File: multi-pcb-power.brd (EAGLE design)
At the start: 51.7 x 36.8 mm, 22 parts, among them Q5 TIP136, T2 BC618, X1 2.52B-ZR, X2 2.52B-ZR, X3 2.52B-ZR, X4 2.54B-ZR

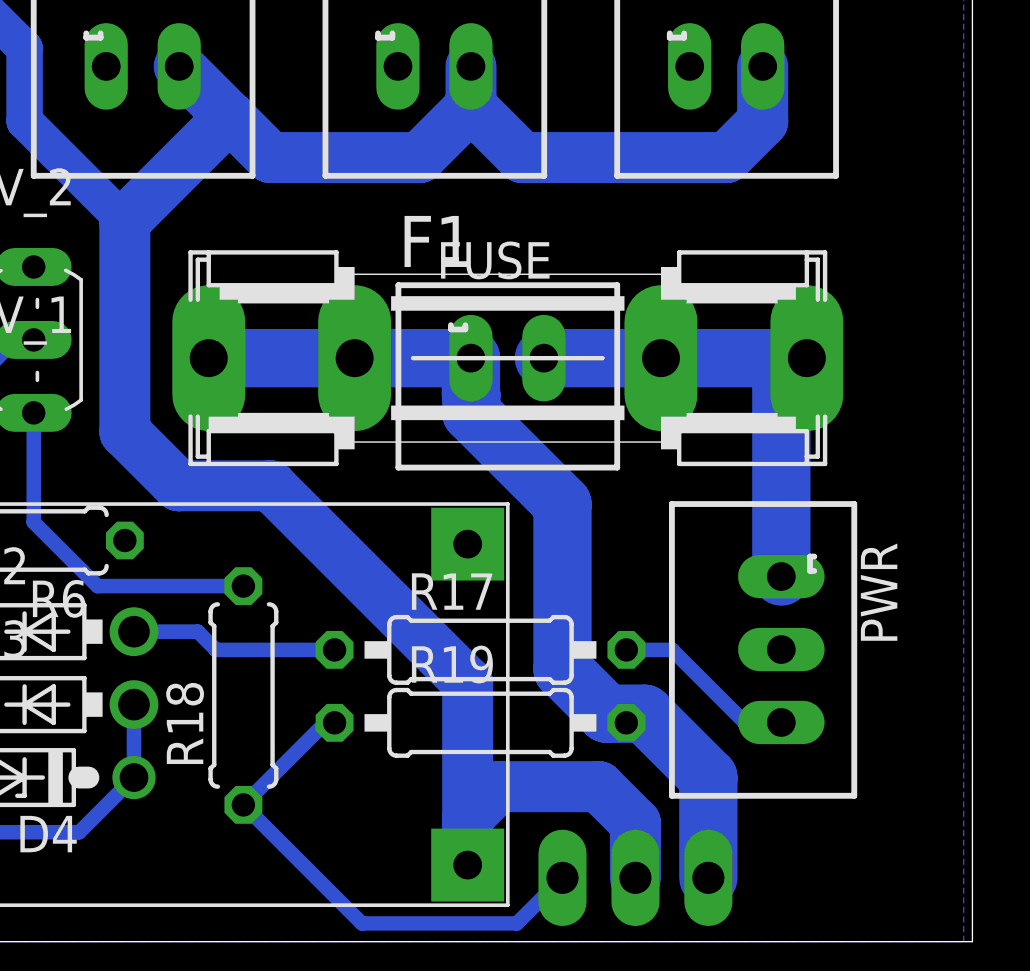
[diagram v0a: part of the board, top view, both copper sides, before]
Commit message: some minor allignment improvement of fuse and power connector
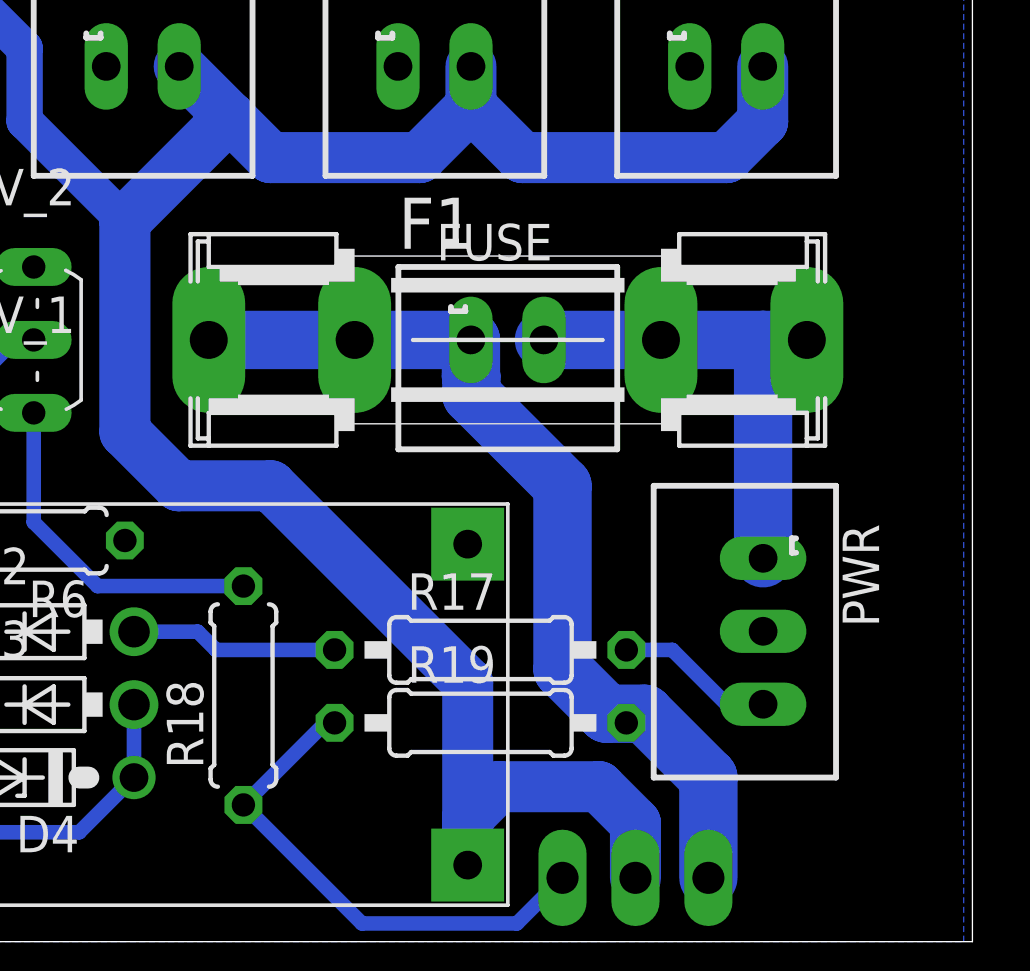
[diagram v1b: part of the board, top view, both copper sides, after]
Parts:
- moved PWR 0.90 mm to (44.5, 10.8)
- moved F1 0.63 mm to (35.6, 21.0)
- moved FUSE 0.63 mm to (35.6, 21.0)
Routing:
- net IGNITION: track 6.44 -> 5.55 mm
- net N$21: track 32.2 -> 32.8 mm
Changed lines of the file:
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@@
 <attribute name="VALUE" x="20.6375" y="8.1915" size="1.27" layer="27" ratio="10" rot="R180"/>
 </element>
-<element name="FUSE" library="con-jst-custom" package="B2B-ZR2.5" value="2.52B-ZR" x="35.56" y="20.32" smashed="yes">
-<attribute name="NAME" x="33.08" y="23.09" size="1.27" layer="25"/>
-<attribute name="VALUE" x="33.08" y="14.28" size="1.27" layer="27"/>
+<element name="FUSE" library="con-jst-custom" package="B2B-ZR2.5" value="2.52B-ZR" x="35.56" y="20.955" smashed="yes">
+<attribute name="NAME" x="33.08" y="23.725" size="1.27" layer="25"/>
+<attribute name="VALUE" x="33.08" y="14.915" size="1.27" layer="27"/>
 </element>
 <element name="JP_PWR_12V" library="pinhead" library_urn="urn:adsk.eagle:library:325" package="1X02" package3d_urn="urn:adsk.eagle:package:22435/2" value="" x="6.0325" y="19.3675" smashed="yes" rot="R180">
@@
 <attribute name="VALUE" x="10.16" y="20.6375" size="1.27" layer="27"/>
 </element>
-<element name="PWR" library="con-jst-custom" package="B3B-ZR2.5" value="2.53B-ZR" x="45.085" y="10.16" smashed="yes" rot="R270">
-<attribute name="NAME" x="47.855" y="13.91" size="1.27" layer="25" rot="R270"/>
-<attribute name="VALUE" x="39.045" y="13.91" size="1.27" layer="27" rot="R270"/>
+<element name="PWR" library="con-jst-custom" package="B3B-ZR2.5" value="2.53B-ZR" x="44.45" y="10.795" smashed="yes" rot="R270">
+<attribute name="NAME" x="47.22" y="14.545" size="1.27" layer="25" rot="R270"/>
+<attribute name="VALUE" x="38.41" y="14.545" size="1.27" layer="27" rot="R270"/>
 </element>
 <element name="Q5" library="transistor-pnp" library_urn="urn:adsk.eagle:library:399" package="TO220" package3d_urn="urn:adsk.eagle:package:29212/1" value="TIP136" x="40.005" y="-4.1275" smashed="yes" rot="MR180">
@@
 <attribute name="VALUE" x="5.14" y="24.44" size="1.27" layer="27"/>
 </element>
-<element name="F1" library="fuse" library_urn="urn:adsk.eagle:library:233" package="SHK20L" package3d_urn="urn:adsk.eagle:package:14071/1" value="2A" x="35.56" y="20.32" smashed="yes">
-<attribute name="MF" value="" x="35.56" y="20.32" size="1.778" layer="27" display="off"/>
-<attribute name="MPN" value="" x="35.56" y="20.32" size="1.778" layer="27" display="off"/>
-<attribute name="NAME" x="31.75" y="23.495" size="1.778" layer="25" ratio="10"/>
-<attribute name="OC_FARNELL" value="unknown" x="35.56" y="20.32" size="1.778" layer="27" display="off"/>
-<attribute name="OC_NEWARK" value="unknown" x="35.56" y="20.32" size="1.778" layer="27" display="off"/>
-<attribute name="POPULARITY" value="3" x="35.56" y="20.32" size="1.778" layer="27" display="off"/>
-<attribute name="VALUE" x="31.75" y="15.24" size="1.778" layer="27" ratio="10"/>
+<element name="F1" library="fuse" library_urn="urn:adsk.eagle:library:233" package="SHK20L" package3d_urn="urn:adsk.eagle:package:14071/1" value="2A" x="35.56" y="20.955" smashed="yes">
+<attribute name="MF" value="" x="35.56" y="20.955" size="1.778" layer="27" display="off"/>
+<attribute name="MPN" value="" x="35.56" y="20.955" size="1.778" layer="27" display="off"/>
+<attribute name="NAME" x="31.75" y="24.13" size="1.778" layer="25" ratio="10"/>
+<attribute name="OC_FARNELL" value="unknown" x="35.56" y="20.955" size="1.778" layer="27" display="off"/>
+<attribute name="OC_NEWARK" value="unknown" x="35.56" y="20.955" size="1.778" layer="27" display="off"/>
+<attribute name="POPULARITY" value="3" x="35.56" y="20.955" size="1.778" layer="27" display="off"/>
+<attribute name="VALUE" x="31.75" y="15.875" size="1.778" layer="27" ratio="10"/>
 </element>
 </elements>
@@
 <contactref element="FUSE" pad="2"/>
 <contactref element="F1" pad="2A"/>
-<wire x1="45.974" y1="20.32" x2="45.085" y2="20.32" width="2.032" layer="16"/>
-<wire x1="45.085" y1="20.32" x2="36.8166" y2="20.32" width="2.032" layer="16"/>
-<wire x1="45.085" y1="12.7148" x2="45.085" y2="20.32" width="2.032" layer="16"/>
+<wire x1="45.974" y1="20.955" x2="44.45" y2="20.955" width="2.032" layer="16"/>
+<wire x1="44.45" y1="20.955" x2="36.8166" y2="20.955" width="2.032" layer="16"/>
+<wire x1="44.45" y1="13.3498" x2="44.45" y2="20.955" width="2.032" layer="16"/>
 </signal>
 <signal name="PWR_ENABLE">
@@
 <contactref element="PWR" pad="3"/>
 <wire x1="39.6875" y1="10.16" x2="41.2884" y2="10.16" width="0.508" layer="16"/>
-<wire x1="43.815" y1="7.6334" x2="45.085" y2="7.6334" width="0.508" layer="16"/>
-<wire x1="43.815" y1="7.6334" x2="41.2884" y2="10.16" width="0.508" layer="16"/>
+<wire x1="43.18" y1="8.2684" x2="44.45" y2="8.2684" width="0.508" layer="16"/>
+<wire x1="43.18" y1="8.2684" x2="41.2884" y2="10.16" width="0.508" layer="16"/>
 </signal>
 <signal name="N$5">
@@
 <contactref element="FUSE" pad="1"/>
 <contactref element="F1" pad="1A"/>
-<wire x1="34.2752" y1="20.32" x2="25.146" y2="20.32" width="2.032" layer="16"/>
-<wire x1="34.2752" y1="20.32" x2="34.2752" y2="19.0648" width="2.032" layer="16"/>
-<wire x1="34.2752" y1="19.0648" x2="34.29" y2="19.05" width="2.032" layer="16"/>
-<wire x1="34.29" y1="19.05" x2="34.29" y2="18.415" width="2.032" layer="16"/>
-<wire x1="34.29" y1="18.415" x2="37.465" y2="15.24" width="2.032" layer="16"/>
-<wire x1="37.465" y1="9.47868125" x2="37.465" y2="15.24" width="2.032" layer="16"/>
+<wire x1="34.2752" y1="20.955" x2="25.146" y2="20.955" width="2.032" layer="16"/>
+<wire x1="34.2752" y1="20.955" x2="34.2752" y2="19.6998" width="2.032" layer="16"/>
+<wire x1="34.2752" y1="19.6998" x2="34.29" y2="19.685" width="2.032" layer="16"/>
+<wire x1="34.29" y1="19.685" x2="34.29" y2="19.05" width="2.032" layer="16"/>
+<wire x1="34.29" y1="19.05" x2="37.465" y2="15.875" width="2.032" layer="16"/>
+<wire x1="37.465" y1="9.47868125" x2="37.465" y2="15.875" width="2.032" layer="16"/>
 <wire x1="42.545" y1="5.715" x2="40.3225" y2="7.9375" width="2.032" layer="16"/>
 <wire x1="39.00618125" y1="7.9375" x2="37.465" y2="9.47868125" width="2.032" layer="16"/>

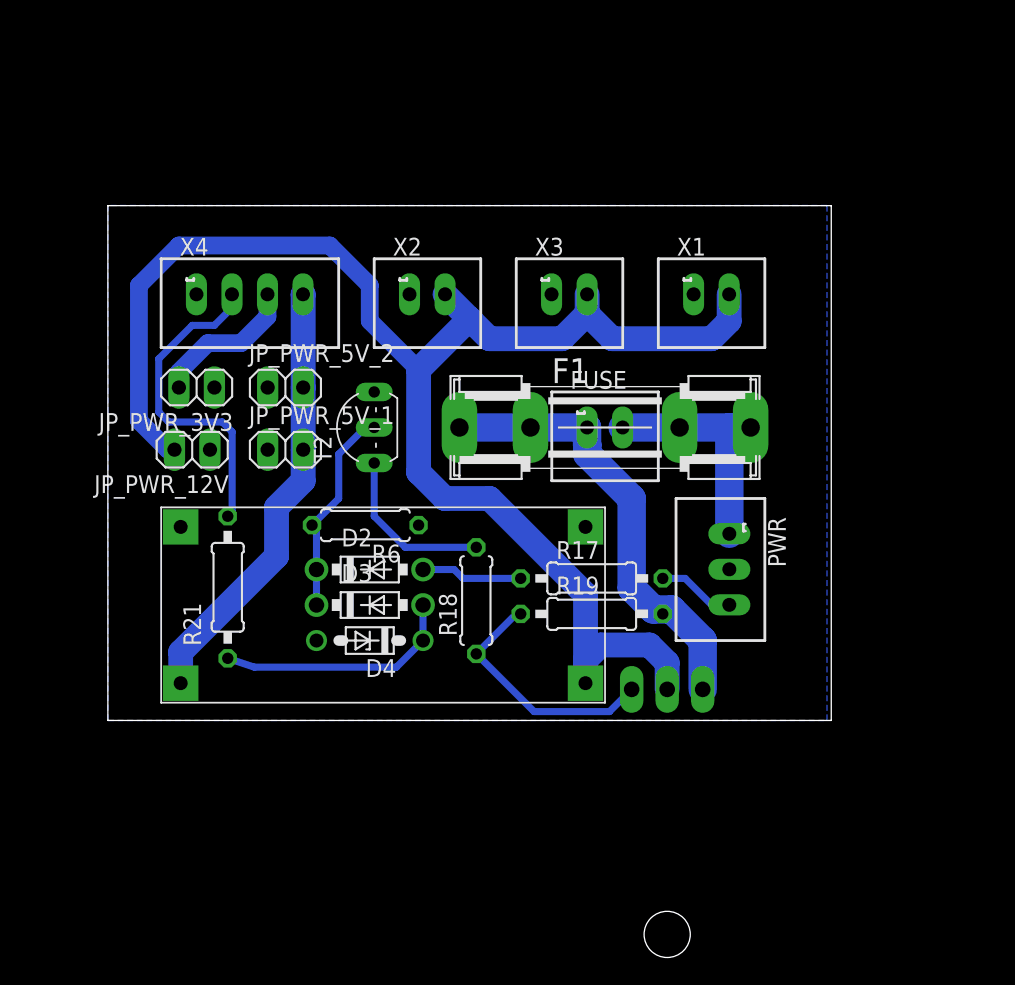
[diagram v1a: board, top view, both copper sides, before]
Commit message: Updated layout of power circuit board
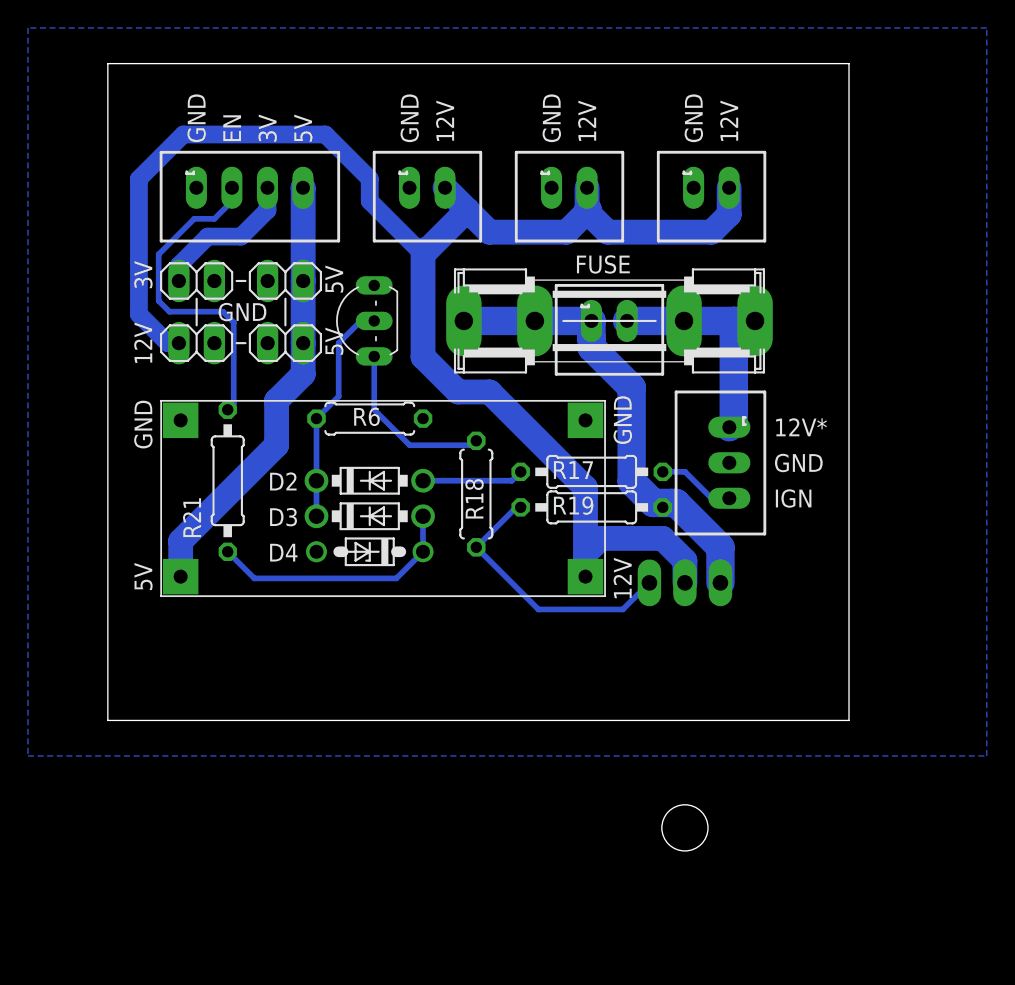
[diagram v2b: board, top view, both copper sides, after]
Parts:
- moved Q5 7.73 mm to (41.3, 3.49)
- moved F1 7.63 mm to (35.9, 28.6)
- moved FUSE 7.63 mm to (35.9, 28.6)
- moved JP_PWR_12V 7.63 mm to (6.35, 27.0)
- moved R6 7.63 mm to (18.7, 21.6)
- moved JP_PWR_3V3 7.62 mm to (6.35, 31.4)
- moved JP_PWR_5V_1 7.62 mm to (12.7, 27.0)
- moved JP_PWR_5V_2 7.62 mm to (12.7, 31.4)
- moved R17 7.62 mm to (34.6, 17.8)
- moved T2 7.62 mm to (17.8, 28.6)
- moved U$4 7.62 mm to (20.3, 16.5)
- moved X1 7.62 mm to (43.2, 38.1)
- moved X2 7.62 mm to (22.9, 38.1)
- moved X3 7.62 mm to (33.0, 38.1)
- moved X4 7.62 mm to (10.2, 38.1)
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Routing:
- net N$14: track 17.8 -> 19.4 mm
- net N$5: track 15.0 -> 16.2 mm
- net N$11: track 17.4 -> 18.1 mm
- net PWR_IN+: track 111.1 -> 111.8 mm
- net N$21: track 32.8 -> 33.4 mm
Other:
- board size 51.7 x 36.8 mm -> 53 x 47 mm
- board text added: "12V"
- board text added: "12V*"
- board text added: "3V"
- board text added: "5V"
- board text added: "EN"
- board text added: "GND"
- board text added: "IGN"
